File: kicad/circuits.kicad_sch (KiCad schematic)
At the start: 36 parts

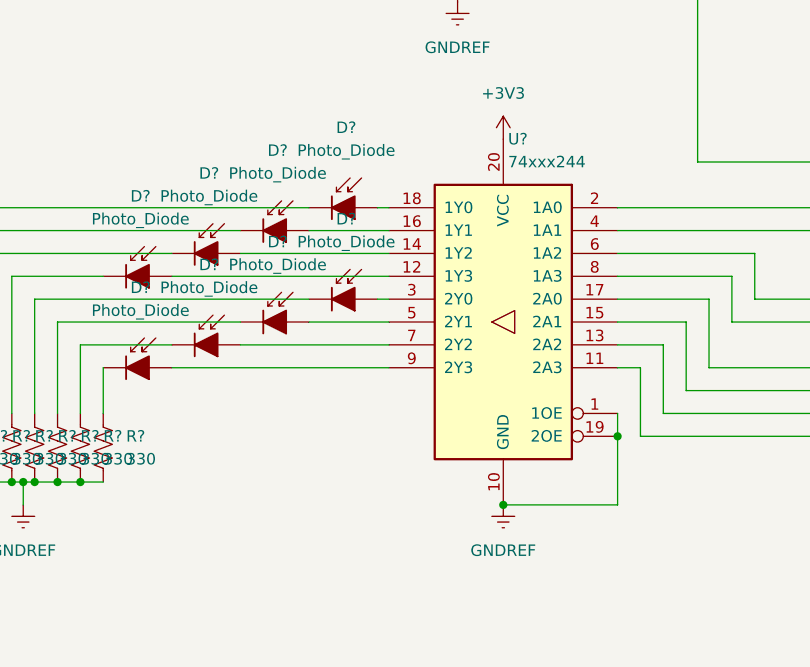
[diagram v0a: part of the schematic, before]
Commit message: Include 218 baselib in kicad directory
* Also added 744 cap

TODO
* Finish 744 to LED bars wiring
* Configure and map PIC32 pins to bar positions
* Light up bars by encoder bin
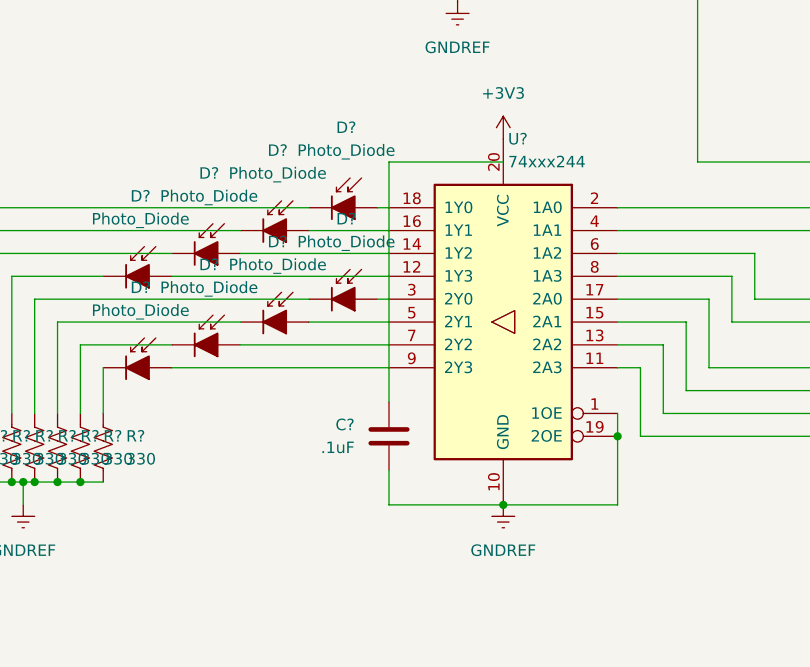
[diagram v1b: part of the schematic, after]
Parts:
- added C?: .1uF, symbol 218 spdl:Cap
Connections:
- net GNDREF: now also C?.1
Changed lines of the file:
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@@
+    (stroke (width 0) (type default) (color 0 0 0 0))
+  )
+  (wire (pts (xy 66.04 48.26) (xy 66.04 74.93))
     (stroke (width 0) (type default) (color 0 0 0 0))
   )
@@
     (stroke (width 0) (type default) (color 0 0 0 0))
   )
+  (wire (pts (xy 66.04 82.55) (xy 66.04 86.36))
+    (stroke (width 0) (type default) (color 0 0 0 0))
+  )
   (wire (pts (xy 187.96 52.07) (xy 187.96 46.99))
     (stroke (width 0) (type default) (color 0 0 0 0))
@@
   )
   (wire (pts (xy 91.44 86.36) (xy 78.74 86.36))
+    (stroke (width 0) (type default) (color 0 0 0 0))
+  )
+  (wire (pts (xy 66.04 86.36) (xy 78.74 86.36))
+    (stroke (width 0) (type default) (color 0 0 0 0))
+  )
+  (wire (pts (xy 78.74 48.26) (xy 66.04 48.26))
     (stroke (width 0) (type default) (color 0 0 0 0))
   )
@@
     (pin "2")
   )
+  (symbol (lib_id "218 spdl:Cap") (at 66.04 78.74 180) (unit 1)
+    (in_bom yes) (on_board yes) (fields_autoplaced)
+    (property "Reference" "C?" (id 0) (at 62.23 77.4699 0)
+      (effects (font (size 1.27 1.27)) (justify left))
+    )
+    (property "Value" ".1uF" (id 1) (at 62.23 80.0099 0)
+      (effects (font (size 1.27 1.27)) (justify left))
+    )
+    (property "Footprint" "" (id 2) (at 65.0748 74.93 0)
+      (effects (font (size 1.27 1.27)) hide)
+    )
+    (property "Datasheet" "" (id 3) (at 66.04 78.74 0)
+      (effects (font (size 1.27 1.27)) hide)
+    )
+    (pin "1")
+    (pin "2")
+  )
   (symbol (lib_id "218:Res1") (at 21.59 80.01 0) (unit 1)
     (in_bom yes) (on_board yes) (fields_autoplaced)
@@
       (reference "C?") (unit 1) (value "0.1uF") (footprint "")
     )
+    (path "/91e5eb7c-3164-46cf-b20c-7852f3cea814"
+      (reference "C?") (unit 1) (value ".1uF") (footprint "")
+    )
     (path "/be7d10c0-f614-4362-ae03-39485d4b37a7"

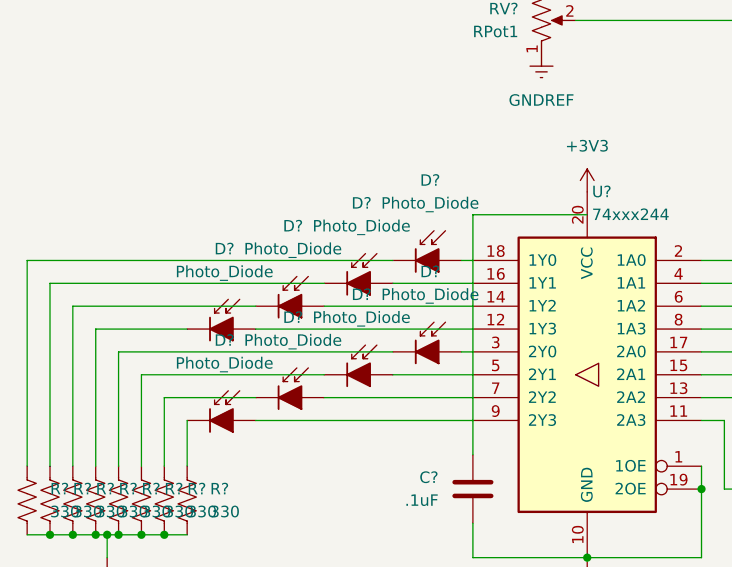
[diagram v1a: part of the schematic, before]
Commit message: Light up more LED bars with longer periods
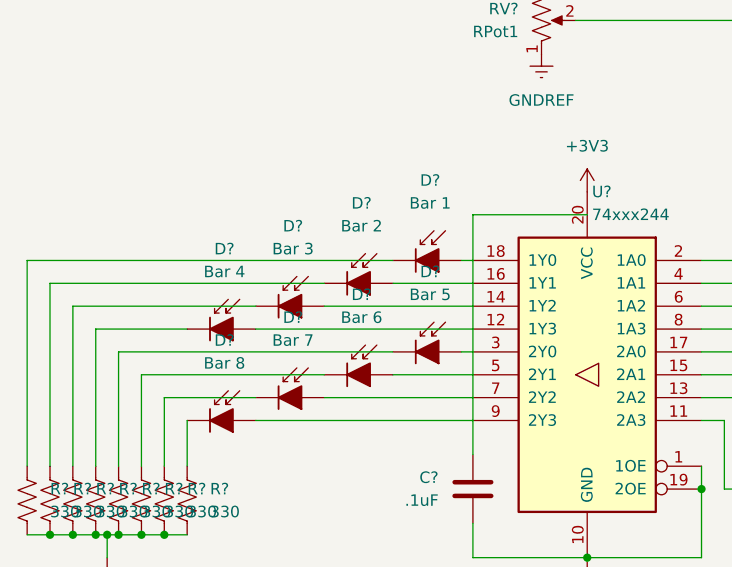
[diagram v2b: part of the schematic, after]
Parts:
- D?: value Photo_Diode -> Bar 4
- D?: value Photo_Diode -> Bar 3
- D?: value Photo_Diode -> Bar 2
- D?: value Photo_Diode -> Bar 7
- D?: value Photo_Diode -> Bar 5
- D?: value Photo_Diode -> Bar 8
- D?: value Photo_Diode -> Bar 1
- D?: value Photo_Diode -> Bar 6
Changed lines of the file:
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@@
     (in_bom yes) (on_board yes) (fields_autoplaced)
     (property "Reference" "D?" (id 0) (at 38.4302 52.07 0))
-    (property "Value" "Photo_Diode" (id 1) (at 38.4302 54.61 0))
+    (property "Value" "Bar 4" (id 1) (at 38.4302 54.61 0))
     (property "Footprint" "" (id 2) (at 38.1 60.96 0)
       (effects (font (size 1.27 1.27)) hide)
@@
     (in_bom yes) (on_board yes) (fields_autoplaced)
     (property "Reference" "D?" (id 0) (at 46.0502 49.53 0))
-    (property "Value" "Photo_Diode" (id 1) (at 46.0502 52.07 0))
+    (property "Value" "Bar 3" (id 1) (at 46.0502 52.07 0))
     (property "Footprint" "" (id 2) (at 45.72 58.42 0)
       (effects (font (size 1.27 1.27)) hide)
@@
     (in_bom yes) (on_board yes) (fields_autoplaced)
     (property "Reference" "D?" (id 0) (at 53.6702 46.99 0))
-    (property "Value" "Photo_Diode" (id 1) (at 53.6702 49.53 0))
+    (property "Value" "Bar 2" (id 1) (at 53.6702 49.53 0))
     (property "Footprint" "" (id 2) (at 53.34 55.88 0)
       (effects (font (size 1.27 1.27)) hide)
@@
     (in_bom yes) (on_board yes) (fields_autoplaced)
     (property "Reference" "D?" (id 0) (at 46.0502 59.69 0))
-    (property "Value" "Photo_Diode" (id 1) (at 46.0502 62.23 0))
+    (property "Value" "Bar 7" (id 1) (at 46.0502 62.23 0))
     (property "Footprint" "" (id 2) (at 45.72 68.58 0)
       (effects (font (size 1.27 1.27)) hide)
@@
     (in_bom yes) (on_board yes) (fields_autoplaced)
     (property "Reference" "D?" (id 0) (at 61.2902 54.61 0))
-    (property "Value" "Photo_Diode" (id 1) (at 61.2902 57.15 0))
+    (property "Value" "Bar 5" (id 1) (at 61.2902 57.15 0))
     (property "Footprint" "" (id 2) (at 60.96 63.5 0)
       (effects (font (size 1.27 1.27)) hide)
@@
     (in_bom yes) (on_board yes) (fields_autoplaced)
     (property "Reference" "D?" (id 0) (at 38.4302 62.23 0))
-    (property "Value" "Photo_Diode" (id 1) (at 38.4302 64.77 0))
+    (property "Value" "Bar 8" (id 1) (at 38.4302 64.77 0))
     (property "Footprint" "" (id 2) (at 38.1 71.12 0)
       (effects (font (size 1.27 1.27)) hide)
@@
     (in_bom yes) (on_board yes) (fields_autoplaced)
     (property "Reference" "D?" (id 0) (at 61.2902 44.45 0))
-    (property "Value" "Photo_Diode" (id 1) (at 61.2902 46.99 0))
+    (property "Value" "Bar 1" (id 1) (at 61.2902 46.99 0))
     (property "Footprint" "" (id 2) (at 60.96 53.34 0)
       (effects (font (size 1.27 1.27)) hide)
@@
     (in_bom yes) (on_board yes) (fields_autoplaced)
     (property "Reference" "D?" (id 0) (at 53.6702 57.15 0))
-    (property "Value" "Photo_Diode" (id 1) (at 53.6702 59.69 0))
+    (property "Value" "Bar 6" (id 1) (at 53.6702 59.69 0))
     (property "Footprint" "" (id 2) (at 53.34 66.04 0)
       (effects (font (size 1.27 1.27)) hide)
@@
     )
     (path "/1856c4db-6bc5-4aa6-8561-35e0b863cdc3"
-      (reference "D?") (unit 1) (value "Photo_Diode") (footprint "")
+      (reference "D?") (unit 1) (value "Bar 4") (footprint "")
     )
     (path "/1e10a410-d7f9-4e57-a739-e558eeccbef9"
@@
     )
     (path "/65833e75-7d61-4f26-bfc3-036f2f5bcdf3"
-      (reference "D?") (unit 1) (value "Photo_Diode") (footprint "")
+      (reference "D?") (unit 1) (value "Bar 3") (footprint "")
     )
     (path "/6aef78d5-6940-4d30-979c-0f79124299cc"
-      (reference "D?") (unit 1) (value "Photo_Diode") (footprint "")
+      (reference "D?") (unit 1) (value "Bar 2") (footprint "")
     )
     (path "/749e9ced-832d-4968-a4d8-fbd2f38bdfa4"
-      (reference "D?") (unit 1) (value "Photo_Diode") (footprint "")
+      (reference "D?") (unit 1) (value "Bar 7") (footprint "")
     )
     (path "/7cc9c8fd-86de-4a56-9387-d0c4ff0214c8"
-      (reference "D?") (unit 1) (value "Photo_Diode") (footprint "")
+      (reference "D?") (unit 1) (value "Bar 5") (footprint "")
     )
     (path "/83e94a5f-5998-4511-bdf9-94881c8efcd0"
@@
     )
     (path "/8d49025e-3e80-4de0-b0a4-15fd10ddddff"
-      (reference "D?") (unit 1) (value "Photo_Diode") (footprint "")
+      (reference "D?") (unit 1) (value "Bar 8") (footprint "")
     )
     (path "/ac118fa7-aadd-4132-bcde-958986661ac2"
-      (reference "D?") (unit 1) (value "Photo_Diode") (footprint "")
+      (reference "D?") (unit 1) (value "Bar 1") (footprint "")
     )
     (path "/dc7f9492-3bf1-4a3a-964f-f93f7a3300df"
@@
     )
     (path "/f7ef616f-5bd7-47cd-87ca-01aa02244537"
-      (reference "D?") (unit 1) (value "Photo_Diode") (footprint "")
+      (reference "D?") (unit 1) (value "Bar 6") (footprint "")
     )
     (path "/b2fd69e6-7066-4cb7-813b-6430b759c6be"

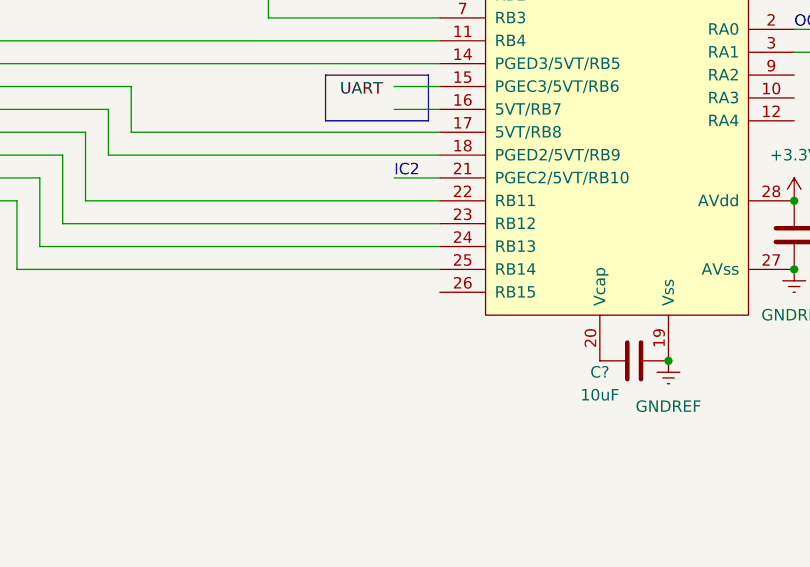
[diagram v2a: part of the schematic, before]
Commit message: Calculate and print RPM
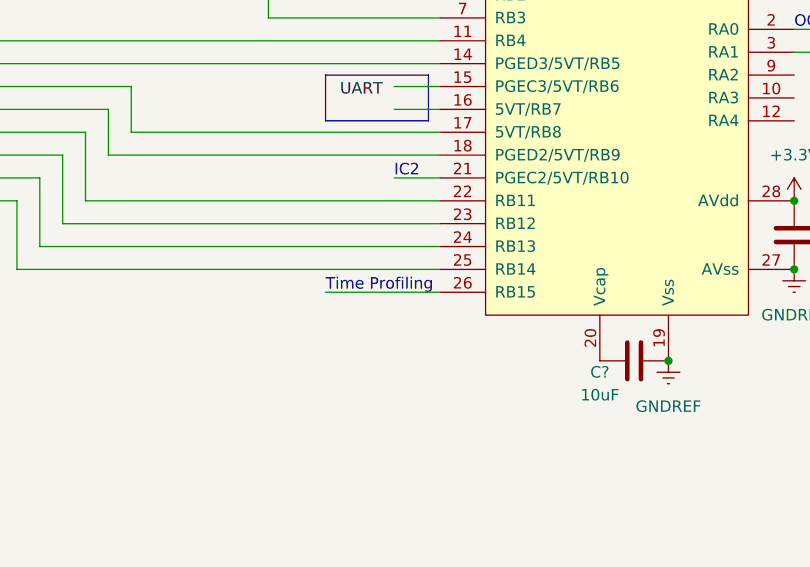
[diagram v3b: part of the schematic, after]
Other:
- note added: "Time Profiling"
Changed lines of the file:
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@@
+    (stroke (width 0) (type default) (color 0 0 0 0))
+  )
+  (wire (pts (xy 128.27 81.28) (xy 140.97 81.28))
     (stroke (width 0) (type default) (color 0 0 0 0))
   )
@@
     (effects (font (size 1.27 1.27)) (justify left bottom))
   )
+  (text "Time Profiling" (at 128.27 81.28 0)
+    (effects (font (size 1.27 1.27)) (justify left bottom))
+  )

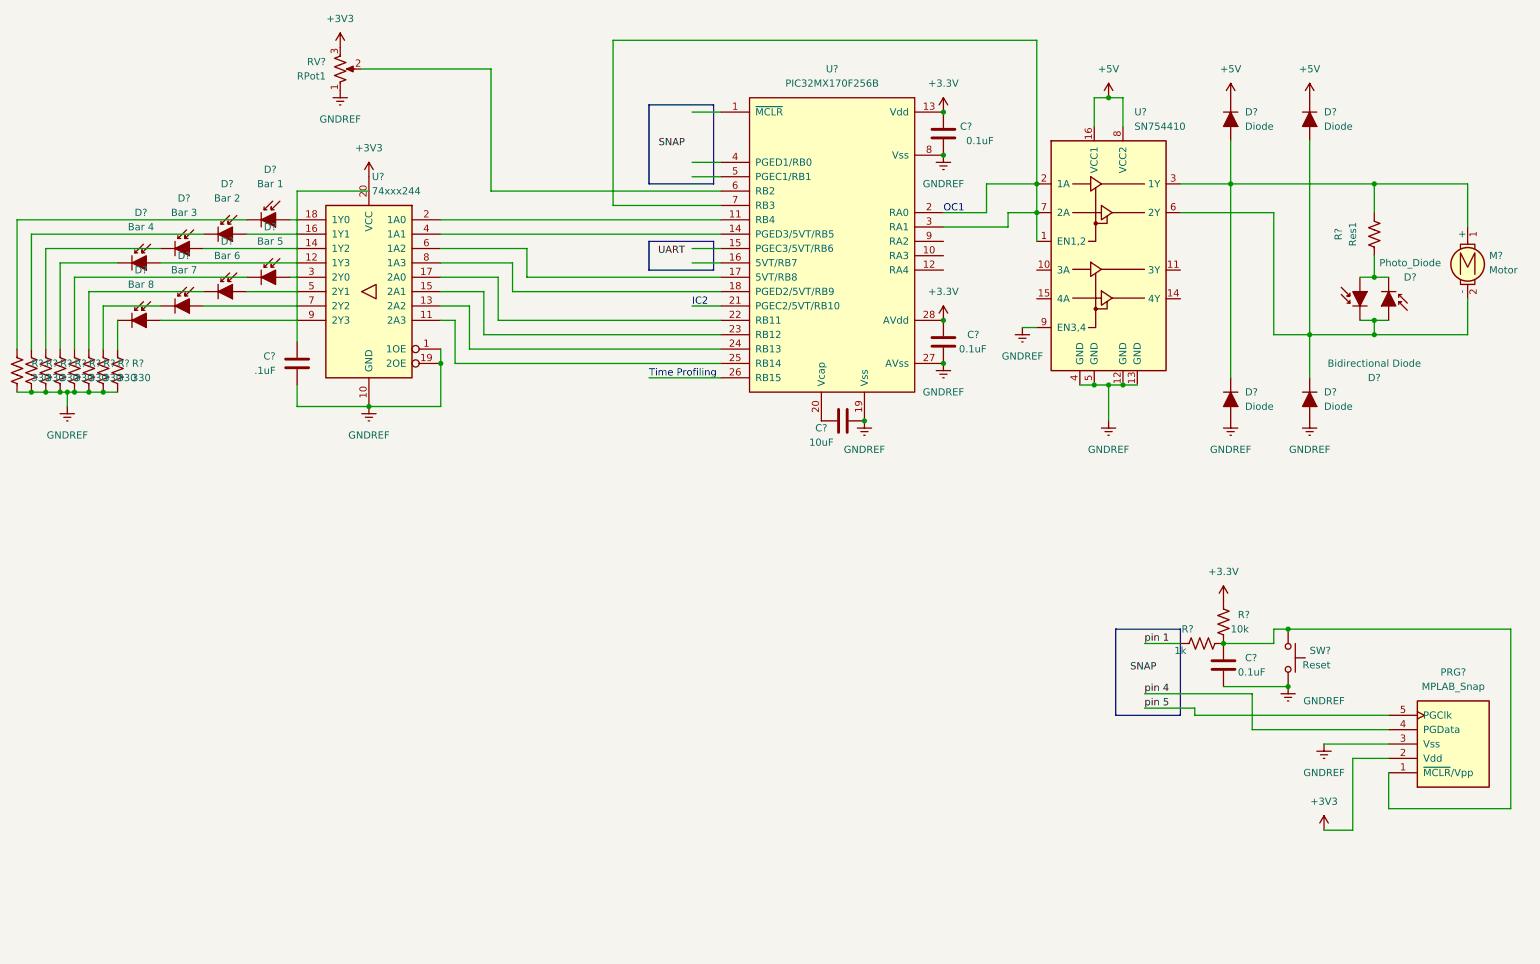
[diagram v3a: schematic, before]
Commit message: Update schematic to measure motor time constant
TODO
* Rewire circuit for 7.1 + remove bi LED (unwanted extra resistance)
* Measure ext and int resistors and update schematic
* Connect probe 1 to PWM and probe 2 to ext resistor
* Measure rise time
* Do design calculations for suitable components
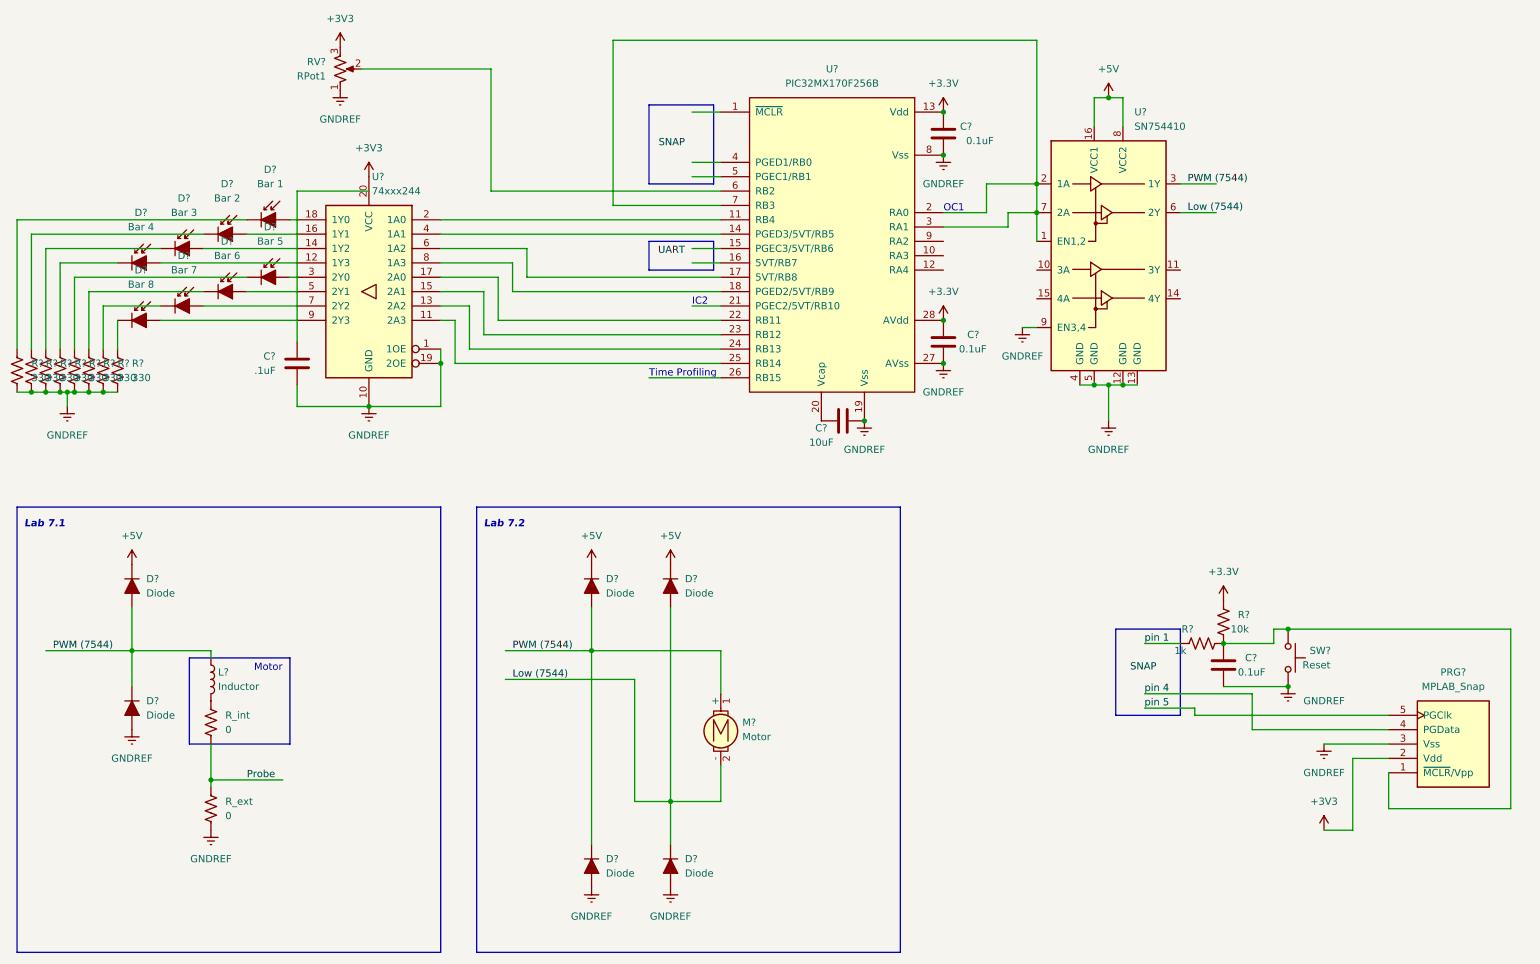
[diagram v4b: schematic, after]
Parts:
- removed D? (x4): Diode, symbol 218:Diode
- removed D?: Photo_Diode, symbol ME218_BaseLib:Photo_Diode
- removed D?: Bidirectional Diode, symbol ME218_BaseLib:Photo_Diode
- removed M?: Motor, symbol 218:Motor
- removed R?: Res1, symbol ME218_BaseLib:Res1
- added D? (x6): Diode, symbol 218:Diode
- added L?: Inductor, symbol 218 spdl:Inductor
- added M?: Motor, symbol 218:Motor
- added R_ext, R_int: 0, symbol 218 spdl:Res1
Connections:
- net +5V: now also D?.1 (K), D?.1 (K), D?.1 (K)
- net GNDREF: now also D?.2 (A), D?.2 (A), D?.2 (A), R_ext.2
- net Low (7544): now reaches U?.6 (2Y)
- net Low (7544): now also D?.1 (K), D?.2 (A), M?.2 (-)
- net PWM (7544): now reaches U?.3 (1Y)
- net PWM (7544): now also D?.1 (K), D?.1 (K), D?.2 (A), D?.2 (A), L?.1, M?.1 (+)
- new net: L?.2, R_int.1
- new net Probe: R_ext.1, R_int.2
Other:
- note added: "Lab 7.1"
- note added: "Lab 7.2"
- note added: "Motor"
